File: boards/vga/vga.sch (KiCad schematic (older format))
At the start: 70 parts, among them J1 Conn_02x20_Odd_Even, Q1 BSS84AK, U1 SN74LV161APW, U10 62256-TSOP, U11 SN74LV161APW, U12 SN74LV161APW, U13 SN74LV244APW, U14 SN74LV20APW, U15 74LV32APWJ, U16 74LV08APWJ, U17 AT28C256-PLCC32, U18 SN74LV273APW, U19 SN74LV273APW, U2 SN74LV161APW, U20 CD74AC151M96, U21 SN74LV157APW, U22 SN74LV10APW, U23 SN74LV74APW, U24 SN74LV00APW, U25 74LV32APWJ, U26 SN74LV21APW, U27 SN74AHC1G86DBVR, U28 74LV32APWJ, U29 74LV08APWJ, U3 SN74LV157APW, U30 SN74LV74APW, U4 SN74LV157APW, U5 SN74LV157APW, U6 SN74LV161APW, U7 SN74LV161APW, U8 SN74LV244APW, U9 62256-TSOP, X1 MXO45HS-3C-25M1750

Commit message: VGA connector
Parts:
- added J2: L77HDE15SD1CH4RHNVGA, Connector_Dsub:DSUB-15-HD_Female_Horizontal_P2.29x1.98mm_EdgePinOffset8.35mm_Housed_MountingHolesOffset10.89mm, symbol Connector:DB15_Female_HighDensity_MountingHoles
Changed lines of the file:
@@
 Wire Bus Line
 	6050 4500 6050 10250
+$Comp
+L Connector:DB15_Female_HighDensity_MountingHoles J2
+U 1 1 608A11F3
+P 21800 4400
+F 0 "J2" H 21800 5267 50  0000 C CNN
+F 1 "L77HDE15SD1CH4RHNVGA" H 21800 5176 50  0000 C CNN
+F 2 "Connector_Dsub:DSUB-15-HD_Female_Horizontal_P2.29x1.98mm_EdgePinOffset8.35mm_Housed_MountingHolesOffset10.89mm" H 20850 4800 50  0001 C CNN
+F 3 " ~" H 20850 4800 50  0001 C CNN
+	1    21800 4400
+	1    0    0    -1
+$EndComp
 $EndSCHEMATC

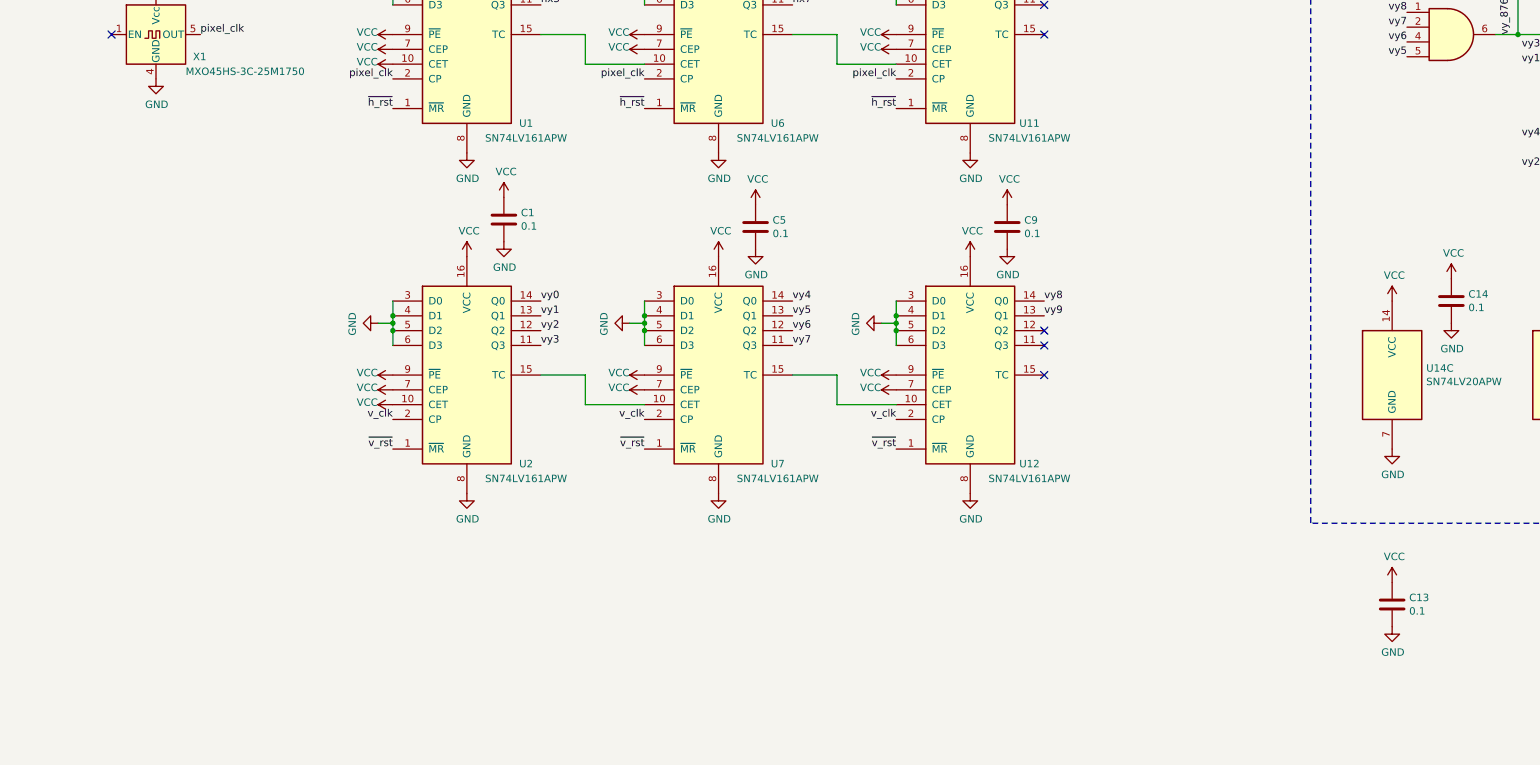
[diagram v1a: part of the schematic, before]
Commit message: VGA board started: connectors and dimensions
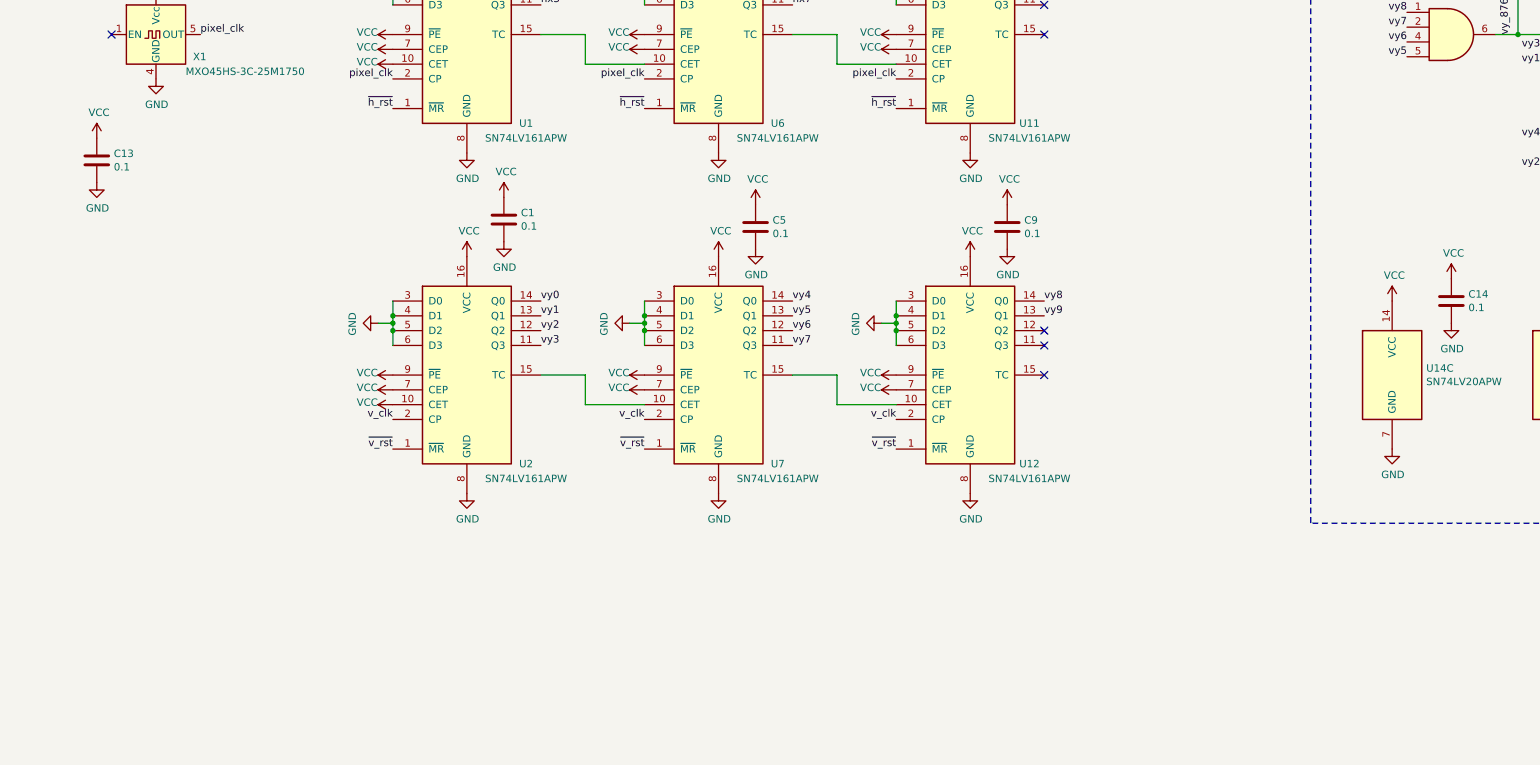
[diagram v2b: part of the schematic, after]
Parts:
- H1, H2, H3, H4: footprint (none) -> MountingHole:MountingHole_3.2mm_M3
- J1: footprint (none) -> Connector_PinHeader_2.54mm:PinHeader_2x20_P2.54mm_Horizontal
- U17: footprint (none) -> missing:PLCC-32_SMD_Socket
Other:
- moved on the sheet: C13
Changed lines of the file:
@@
 F 0 "H1" H 800 696 50  0000 L CNN
 F 1 "MountingHole" H 800 605 50  0000 L CNN
-F 2 "" H 700 650 50  0001 C CNN
+F 2 "MountingHole:MountingHole_3.2mm_M3" H 700 650 50  0001 C CNN
 F 3 "~" H 700 650 50  0001 C CNN
 	1    700  650
@@
 F 0 "H4" H 22400 746 50  0000 L CNN
 F 1 "MountingHole" H 22400 655 50  0000 L CNN
-F 2 "" H 22300 700 50  0001 C CNN
+F 2 "MountingHole:MountingHole_3.2mm_M3" H 22300 700 50  0001 C CNN
 F 3 "~" H 22300 700 50  0001 C CNN
 	1    22300 700
@@
 F 0 "H2" H 900 31346 50  0000 L CNN
 F 1 "MountingHole" H 900 31255 50  0000 L CNN
-F 2 "" H 800 31300 50  0001 C CNN
+F 2 "MountingHole:MountingHole_3.2mm_M3" H 800 31300 50  0001 C CNN
 F 3 "~" H 800 31300 50  0001 C CNN
 	1    800  31300
@@
 F 0 "H3" H 22250 31046 50  0000 L CNN
 F 1 "MountingHole" H 22250 30955 50  0000 L CNN
-F 2 "" H 22150 31000 50  0001 C CNN
+F 2 "MountingHole:MountingHole_3.2mm_M3" H 22150 31000 50  0001 C CNN
 F 3 "~" H 22150 31000 50  0001 C CNN
 	1    22150 31000
@@
 F 0 "J1" H 1800 7167 50  0000 C CNN
 F 1 "Conn_02x20_Odd_Even" H 1800 7076 50  0000 C CNN
-F 2 "" H 1750 6050 50  0001 C CNN
+F 2 "Connector_PinHeader_2.54mm:PinHeader_2x20_P2.54mm_Horizontal" H 1750 6050 50  0001 C CNN
 F 3 "~" H 1750 6050 50  0001 C CNN
 	1    1750 6050
@@
 F 0 "U17" H 12400 4600 50  0000 C CNN
 F 1 "AT28C256-PLCC32" H 12400 4450 50  0000 C CNN
-F 2 "" H 12200 5900 50  0001 C CNN
+F 2 "missing:PLCC-32_SMD_Socket" H 12200 5900 50  0001 C CNN
 F 3 "http://ww1.microchip.com/downloads/en/DeviceDoc/doc0006.pdf" H 12200 5900 50  0001 C CNN
 	1    11950 5550
@@
 L Device:C C13
 U 1 1 604933C0
-P 9950 17700
-F 0 "C13" H 10065 17746 50  0000 L CNN
-F 1 "0.1" H 10065 17655 50  0000 L CNN
-F 2 "Capacitor_SMD:C_0805_2012Metric" H 9988 17550 50  0001 C CNN
-F 3 "~" H 9950 17700 50  0001 C CNN
-	1    9950 17700
+P 1200 14700
+F 0 "C13" H 1315 14746 50  0000 L CNN
+F 1 "0.1" H 1315 14655 50  0000 L CNN
+F 2 "Capacitor_SMD:C_0805_2012Metric" H 1238 14550 50  0001 C CNN
+F 3 "~" H 1200 14700 50  0001 C CNN
+	1    1200 14700
 	1    0    0    -1
 $EndComp
@@
 L power:GND #PWR0105
 U 1 1 604939A9
-P 9950 17850
-F 0 "#PWR0105" H 9950 17600 50  0001 C CNN
-F 1 "GND" H 9955 17677 50  0000 C CNN
-F 2 "" H 9950 17850 50  0001 C CNN
-F 3 "" H 9950 17850 50  0001 C CNN
-	1    9950 17850
+P 1200 14850
+F 0 "#PWR0105" H 1200 14600 50  0001 C CNN
+F 1 "GND" H 1205 14677 50  0000 C CNN
+F 2 "" H 1200 14850 50  0001 C CNN
+F 3 "" H 1200 14850 50  0001 C CNN
+	1    1200 14850
 	1    0    0    -1
 $EndComp
@@
 L power:VCC #PWR0104
 U 1 1 6049402E
-P 9950 17550
-F 0 "#PWR0104" H 9950 17400 50  0001 C CNN
-F 1 "VCC" H 9965 17723 50  0000 C CNN
-F 2 "" H 9950 17550 50  0001 C CNN
-F 3 "" H 9950 17550 50  0001 C CNN
-	1    9950 17550
+P 1200 14550
+F 0 "#PWR0104" H 1200 14400 50  0001 C CNN
+F 1 "VCC" H 1215 14723 50  0000 C CNN
+F 2 "" H 1200 14550 50  0001 C CNN
+F 3 "" H 1200 14550 50  0001 C CNN
+	1    1200 14550
 	1    0    0    -1
 $EndComp
@@
 Wire Wire Line
 	16700 5100 16700 4650
+$Comp
+L Connector:DB15_Female_HighDensity_MountingHoles J2
+U 1 1 608A11F3
+P 21800 4400
+F 0 "J2" H 21800 5267 50  0000 C CNN
+F 1 "L77HDE15SD1CH4RHNVGA" H 21800 5176 50  0000 C CNN
+F 2 "Connector_Dsub:DSUB-15-HD_Female_Horizontal_P2.29x1.98mm_EdgePinOffset8.35mm_Housed_MountingHolesOffset10.89mm" H 20850 4800 50  0001 C CNN
+F 3 " ~" H 20850 4800 50  0001 C CNN
+	1    21800 4400
+	1    0    0    -1
+$EndComp
 Wire Bus Line
 	11050 5150 11050 5850
@@
 Wire Bus Line
 	6050 4500 6050 10250
-$Comp
-L Connector:DB15_Female_HighDensity_MountingHoles J2
-U 1 1 608A11F3
-P 21800 4400
-F 0 "J2" H 21800 5267 50  0000 C CNN
-F 1 "L77HDE15SD1CH4RHNVGA" H 21800 5176 50  0000 C CNN
-F 2 "Connector_Dsub:DSUB-15-HD_Female_Horizontal_P2.29x1.98mm_EdgePinOffset8.35mm_Housed_MountingHolesOffset10.89mm" H 20850 4800 50  0001 C CNN
-F 3 " ~" H 20850 4800 50  0001 C CNN
-	1    21800 4400
-	1    0    0    -1
-$EndComp
 $EndSCHEMATC

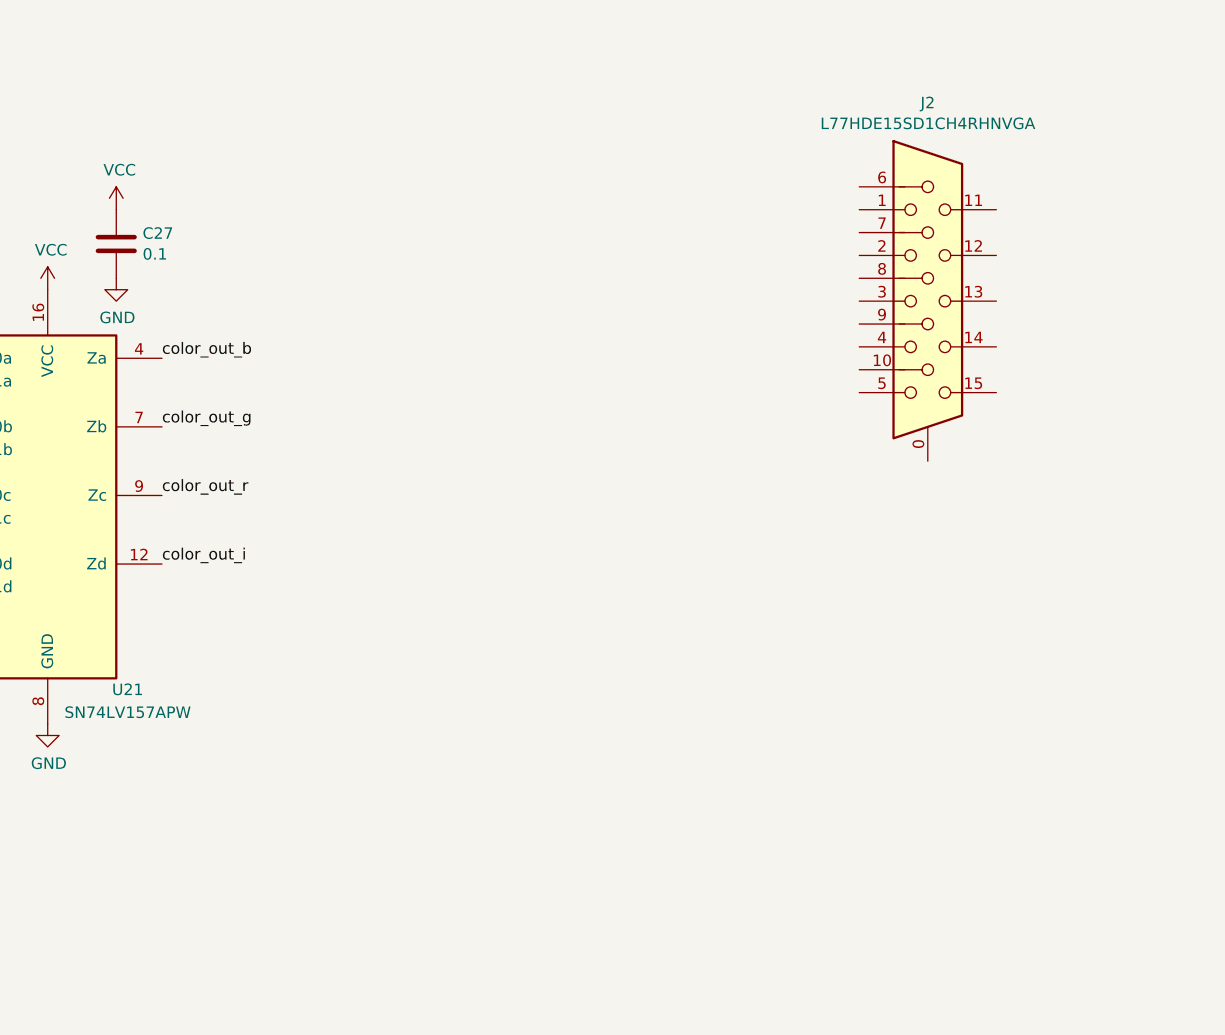
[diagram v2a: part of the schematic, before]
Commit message: VGA: DAC with ideal resistor values
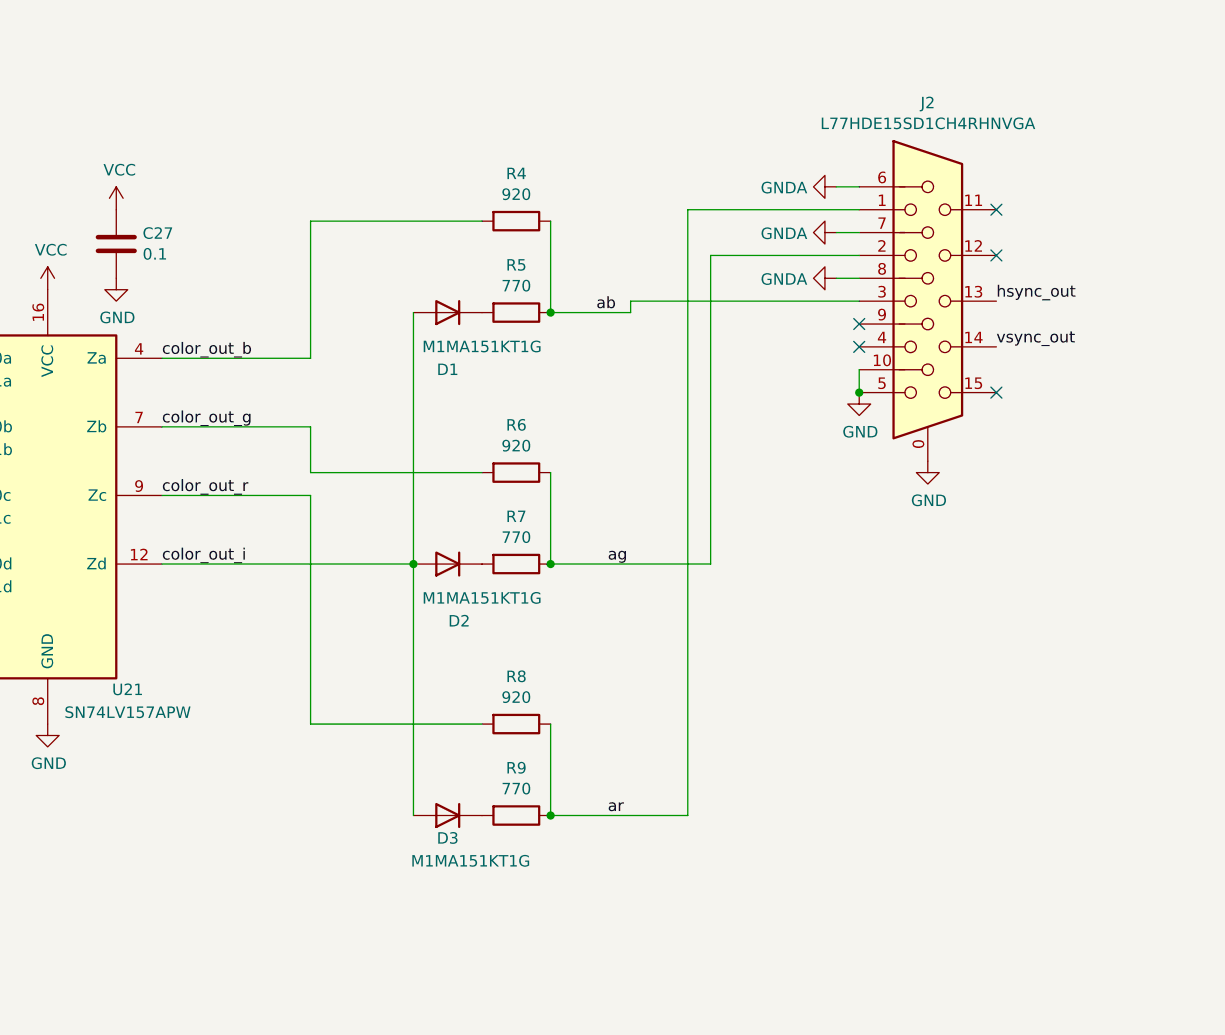
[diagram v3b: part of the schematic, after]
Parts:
- added D1, D2, D3: M1MA151KT1G, Diode_SMD:D_SOT-23_ANK, symbol Device:D
- added R4, R6, R8: 920, symbol Device:R
- added R5, R7, R9: 770, symbol Device:R
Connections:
- net GND: now also J2.0, J2.10, J2.5
- net color_out_b: now also R4.2
- net color_out_g: now also R6.2
- net color_out_i: now also D1.2 (A), D2.2 (A), D3.2 (A)
- net color_out_r: now also R8.2
- net hsync_out: now also J2.13
- net vsync_out: now also J2.14
- net ar: now reaches J2.1
- net ar: now also R8.1, R9.1
- net ag: now reaches J2.2
- net ag: now also R6.1, R7.1
- net ab: now reaches J2.3
- net ab: now also R4.1, R5.1
- net GNDA: now reaches J2.6
- net GNDA: now also J2.7, J2.8
- new net: D1.1 (K), R5.2
- new net: D2.1 (K), R7.2
- new net: D3.1 (K), R9.2
- no-connect marks 20 -> 25
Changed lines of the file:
@@
 	1    0    0    -1
 $EndComp
+NoConn ~ 21500 4600
+$Comp
+L power:GND #PWR0169
+U 1 1 5FE2CDBD
+P 21500 4800
+F 0 "#PWR0169" H 21500 4550 50  0001 C CNN
+F 1 "GND" H 21505 4627 50  0000 C CNN
+F 2 "" H 21500 4800 50  0001 C CNN
+F 3 "" H 21500 4800 50  0001 C CNN
+	1    21500 4800
+	1    0    0    -1
+$EndComp
+Wire Wire Line
+	21500 4700 21500 4800
+Connection ~ 21500 4800
+NoConn ~ 22100 4000
+NoConn ~ 22100 4200
+NoConn ~ 22100 4800
+$Comp
+L power:GND #PWR0170
+U 1 1 5FEA5884
+P 21800 5100
+F 0 "#PWR0170" H 21800 4850 50  0001 C CNN
+F 1 "GND" H 21805 4927 50  0000 C CNN
+F 2 "" H 21800 5100 50  0001 C CNN
+F 3 "" H 21800 5100 50  0001 C CNN
+	1    21800 5100
+	1    0    0    -1
+$EndComp
+Text Label 22100 4400 0    50   ~ 0
+hsync_out
+Text Label 22100 4600 0    50   ~ 0
+vsync_out
+$Comp
+L Device:D D1
+U 1 1 5FEACDCC
+P 19700 4450
+F 0 "D1" H 19700 4700 50  0000 C CNN
+F 1 "M1MA151KT1G" H 19550 4600 50  0000 C CNN
+F 2 "Diode_SMD:D_SOT-23_ANK" H 19700 4450 50  0001 C CNN
+F 3 "https://www.mouser.de/datasheet/2/308/M1MA151KT1_D-1810723.pdf" H 19700 4450 50  0001 C CNN
+	1    19700 4450
+	-1   0    0    1
+$EndComp
+$Comp
+L Device:R R5
+U 1 1 5FEB1B5A
+P 20000 4450
+F 0 "R5" V 19793 4450 50  0000 C CNN
+F 1 "770" V 19884 4450 50  0000 C CNN
+F 2 "" V 19930 4450 50  0001 C CNN
+F 3 "~" H 20000 4450 50  0001 C CNN
+	1    20000 4450
+	0    1    1    0
+$EndComp
+$Comp
+L Device:R R4
+U 1 1 5FEB20CB
+P 20000 4050
+F 0 "R4" V 19793 4050 50  0000 C CNN
+F 1 "920" V 19884 4050 50  0000 C CNN
+F 2 "" V 19930 4050 50  0001 C CNN
+F 3 "~" H 20000 4050 50  0001 C CNN
+	1    20000 4050
+	0    1    1    0
+$EndComp
+Wire Wire Line
+	20150 4450 20150 4050
+Connection ~ 20150 4450
+$Comp
+L power:GNDA #PWR0166
+U 1 1 5FED7D9B
+P 21400 3900
+F 0 "#PWR0166" H 21400 3650 50  0001 C CNN
+F 1 "GNDA" V 21405 3773 50  0000 R CNN
+F 2 "" H 21400 3900 50  0001 C CNN
+F 3 "" H 21400 3900 50  0001 C CNN
+	1    21400 3900
+	0    1    1    0
+$EndComp
+Wire Wire Line
+	21500 3900 21400 3900
+$Comp
+L power:GNDA #PWR0167
+U 1 1 5FEF8336
+P 21400 4100
+F 0 "#PWR0167" H 21400 3850 50  0001 C CNN
+F 1 "GNDA" V 21405 3973 50  0000 R CNN
+F 2 "" H 21400 4100 50  0001 C CNN
+F 3 "" H 21400 4100 50  0001 C CNN
+	1    21400 4100
+	0    1    1    0
+$EndComp
+$Comp
+L power:GNDA #PWR0168
+U 1 1 5FEF86C1
+P 21400 4300
+F 0 "#PWR0168" H 21400 4050 50  0001 C CNN
+F 1 "GNDA" V 21405 4173 50  0000 R CNN
+F 2 "" H 21400 4300 50  0001 C CNN
+F 3 "" H 21400 4300 50  0001 C CNN
+	1    21400 4300
+	0    1    1    0
+$EndComp
+Wire Wire Line
+	21400 4300 21500 4300
+Wire Wire Line
+	21400 4100 21500 4100
+$Comp
+L Device:D D2
+U 1 1 5FF3DA39
+P 19700 5550
+F 0 "D2" H 19650 5800 50  0000 C CNN
+F 1 "M1MA151KT1G" H 19550 5700 50  0000 C CNN
+F 2 "Diode_SMD:D_SOT-23_ANK" H 19700 5550 50  0001 C CNN
+F 3 "https://www.mouser.de/datasheet/2/308/M1MA151KT1_D-1810723.pdf" H 19700 5550 50  0001 C CNN
+	1    19700 5550
+	-1   0    0    1
+$EndComp
+$Comp
+L Device:R R7
+U 1 1 5FF3DA3F
+P 20000 5550
+F 0 "R7" V 19793 5550 50  0000 C CNN
+F 1 "770" V 19884 5550 50  0000 C CNN
+F 2 "" V 19930 5550 50  0001 C CNN
+F 3 "~" H 20000 5550 50  0001 C CNN
+	1    20000 5550
+	0    1    1    0
+$EndComp
+$Comp
+L Device:R R6
+U 1 1 5FF3DA45
+P 20000 5150
+F 0 "R6" V 19793 5150 50  0000 C CNN
+F 1 "920" V 19884 5150 50  0000 C CNN
+F 2 "" V 19930 5150 50  0001 C CNN
+F 3 "~" H 20000 5150 50  0001 C CNN
+	1    20000 5150
+	0    1    1    0
+$EndComp
+Wire Wire Line
+	20150 5550 20150 5150
+Connection ~ 20150 5550
+$Comp
+L Device:D D3
+U 1 1 5FF5B8A0
+P 19700 6650
+F 0 "D3" H 19700 6750 50  0000 C CNN
+F 1 "M1MA151KT1G" H 19600 6850 50  0000 C CNN
+F 2 "Diode_SMD:D_SOT-23_ANK" H 19700 6650 50  0001 C CNN
+F 3 "https://www.mouser.de/datasheet/2/308/M1MA151KT1_D-1810723.pdf" H 19700 6650 50  0001 C CNN
+	1    19700 6650
+	-1   0    0    1
+$EndComp
+$Comp
+L Device:R R9
+U 1 1 5FF5B8A6
+P 20000 6650
+F 0 "R9" V 19793 6650 50  0000 C CNN
+F 1 "770" V 19884 6650 50  0000 C CNN
+F 2 "" V 19930 6650 50  0001 C CNN
+F 3 "~" H 20000 6650 50  0001 C CNN
+	1    20000 6650
+	0    1    1    0
+$EndComp
+$Comp
+L Device:R R8
+U 1 1 5FF5B8AC
+P 20000 6250
+F 0 "R8" V 19793 6250 50  0000 C CNN
+F 1 "920" V 19884 6250 50  0000 C CNN
+F 2 "" V 19930 6250 50  0001 C CNN
+F 3 "~" H 20000 6250 50  0001 C CNN
+	1    20000 6250
+	0    1    1    0
+$EndComp
+Wire Wire Line
+	20150 6650 20150 6250
+Connection ~ 20150 6650
+Wire Wire Line
+	19550 6650 19550 5550
+Connection ~ 19550 5550
+Wire Wire Line
+	19550 5550 19550 4450
+Wire Wire Line
+	19550 5550 18450 5550
+Wire Wire Line
+	19850 6250 19100 6250
+Wire Wire Line
+	19100 6250 19100 5250
+Wire Wire Line
+	19100 5250 18450 5250
+Wire Wire Line
+	19850 5150 19100 5150
+Wire Wire Line
+	19100 5150 19100 4950
+Wire Wire Line
+	19100 4950 18450 4950
+Wire Wire Line
+	19850 4050 19100 4050
+Wire Wire Line
+	19100 4050 19100 4650
+Wire Wire Line
+	19100 4650 18450 4650
+Wire Wire Line
+	21500 4400 20500 4400
+Wire Wire Line
+	20500 4400 20500 4450
+Wire Wire Line
+	20500 4450 20150 4450
+Wire Wire Line
+	21500 4200 20850 4200
+Wire Wire Line
+	20850 4200 20850 5550
+Wire Wire Line
+	20850 5550 20150 5550
+Wire Wire Line
+	20150 6650 20750 6650
+Wire Wire Line
+	20750 6650 20750 4000
+Wire Wire Line
+	20750 4000 21500 4000
+Text Label 20350 4450 0    50   ~ 0
+ab
+Text Label 20400 5550 0    50   ~ 0
+ag
+Text Label 20400 6650 0    50   ~ 0
+ar
+NoConn ~ 21500 4500
 Wire Bus Line
 	11050 5150 11050 5850
